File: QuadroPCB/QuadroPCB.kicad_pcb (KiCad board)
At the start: 2 copper layers, 80 x 119.4 mm, 23 parts, among them IC1 AT24CS02-SSHM, P1 MPU9150, P10 AKKU, P2 stm32discovery_left, P3 stm32discovery_right, P4 rc_signal, P5 Motor3, P6 Motor4, P7 BMP180, P8 Motor1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

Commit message: dei mudder commitet
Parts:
- P10: footprint Wire_Connections_Bridges:WireConnection_1-2mmDrill -> Connect:PINHEAD1-2
- moved R4 15.9 mm to (108.0, 107.3), turned to 90 degrees
- moved Q1 14.8 mm to (108.0, 98.4), turned to 270 degrees
- moved P1 12.0 mm to (72.4, 146.1)
- moved IC1 11.4 mm to (94.0, 142.2), turned to 90 degrees
- moved P7 10.2 mm to (86.4, 166.4)
- moved SP1 6.35 mm to (100.3, 76.2)
- moved R5 4.62 mm to (98.4, 168.9)
- moved R3 2.29 mm to (101.0, 168.9)
- moved P10 1.27 mm to (58.4, 74.9)
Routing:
- net GND: track 38.6 -> 445.8 mm
- net +3V3: track 0.00 -> 174.3 mm
- net +5V: track 30.8 -> 83.3 mm
- net +BATT: track 28.6 -> 73.1 mm
- net I2C1_SDA: track 0.00 -> 38.7 mm
- net I2C1_SCL: track 0.00 -> 36.7 mm
- net PE4: track 0.00 -> 33.0 mm
- net I2C2_SCL: track 0.00 -> 24.1 mm
- net Net-(Q1-Pad3): track 0.00 -> 23.2 mm
- net MOTOR2: track 0.00 -> 22.4 mm
- net I2C2_SDA: track 0.00 -> 22.2 mm
- net PC9: track 0.00 -> 15.9 mm
- net MOTOR3: track 0.00 -> 14.7 mm
- net MOTOR1: track 0.00 -> 13.8 mm
- net RC_Signal: track 0.00 -> 13.8 mm
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- added copper zone on B.Cu, net GND
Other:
- net class Default: clearance 0.254 -> 0.25
- net class bla: clearance 0.254 -> 0.25
- rule trace_clearance: 0.254 -> 0.25

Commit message: neuer step down
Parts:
- added C3: 10nF, Capacitors_SMD:C_0805_HandSoldering, B.Cu at (81.9, 97.2)
- C1: value 100µ 25V -> 220µF 25V; footprint Capacitors_SMD:c_elec_6.3x7.7 -> Capacitors_SMD:c_elec_8x10.5
- C2: value 680µF 10V -> 100µF 10V; footprint Capacitors_SMD:c_elec_8x10 -> Capacitors_SMD:c_elec_8x6.7
- D1: value MBR360 -> MBRS340; footprint Diodes_SMD:Diode-DO-214BA -> Diodes_SMD:Diode-DO-214AB_Handsoldering
- L1: value 220µH -> 33µH 1,4 A; footprint Choke_SMD:Choke_SMD_PISR_Handsoldering_FASTRON -> Choke_SMD:Choke_SMD_PISN_Handsoldering_FASTRON
- U1: value LM2576S-5 -> LM2675M-5; footprint SMD_Packages:TO-263-5_HandSoldering -> SMD_Packages:SOIC-8-N
- moved U1 16.2 mm to (81.9, 102.2)
- moved C2 16.2 mm to (88.3, 111.1), turned to 0 degrees
- moved C1 8.28 mm to (65.4, 88.3), turned to 0 degrees
- moved D1 7.85 mm to (71.8, 101.6)
- moved R1 7.73 mm to (50.8, 118.1), turned to 270 degrees
- moved L1 6.54 mm to (81.9, 88.3)
- moved P10 4.49 mm to (62.9, 75.6), turned to 0 degrees
- moved R2 2.29 mm to (49.5, 122.6), turned to 180 degrees
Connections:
- net I2C2_SDA renamed PA10
- net MOTOR2 renamed PC7
- net MOTOR3 renamed PC8
- net PE4 renamed MPU9150_INT
- D1 pad 1: /pwr -> Net-(C3-Pad1)
- L1 pad 1: /pwr -> Net-(C3-Pad1)
- U1 pad 1: +BATT -> Net-(C3-Pad2)
- U1 pad 2: /pwr -> (no net)
- U1 pad 3: GND -> (no net)
- U1 pad 5: GND -> Net-(U1-Pad5)
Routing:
- net GND: track 445.8 -> 365.2 mm
- net +5V: track 83.3 -> 50.4 mm
- net Net-(C3-Pad1): track 0.00 -> 27.2 mm
- net /pwr: track 18.0 -> 0.00 mm
- net Net-(C3-Pad2): track 0.00 -> 3.97 mm
- net +3V3: track 174.3 -> 172.1 mm
- net +BATT: track 73.1 -> 73.9 mm, vias 0 -> 2
- net ADC_Akkumonitor: track 7.49 -> 8.17 mm
- added copper zone on B.Cu, net +5V
- added copper zone on B.Cu, net Net-(C3-Pad1)

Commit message: blubb
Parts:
- added P11: MeisterFluglicht, Pin_Headers:Pin_Header_Straight_1x05, F.Cu at (72.4, 153.7)
- added Q2: Q_NMOS_GSD, Housings_SOT-23_SOT-143_TSOT-6:SOT-23_Handsoldering, B.Cu at (110.5, 106.7)
- added R6: 1k, Resistors_SMD:R_0805_HandSoldering, B.Cu at (111.8, 113.0)
- added SP2: SPEAKER, Buzzers_Beepers:Buzzer_12x9.5RM7.6, B.Cu at (100.3, 104.1)
- SP1: moved to B.Cu
- moved SP1 12.7 mm to (100.3, 88.9), turned to 270 degrees
- moved R4 11.9 mm to (113.0, 118.1), turned to 0 degrees
- moved C3 5.08 mm to (76.8, 97.2)
- moved L1 5.08 mm to (76.8, 88.3)
- moved U1 5.08 mm to (76.8, 102.2)
- moved P10 5.08 mm to (57.8, 75.6)
- moved C1 5.08 mm to (60.3, 88.3)
- moved C2 5.08 mm to (83.2, 111.1)
- moved D1 5.08 mm to (66.7, 101.6)
- moved Q1 3.17 mm to (108.0, 95.2), turned to 180 degrees
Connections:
- net I2C1_SCL renamed PB6
- net MOTOR1 renamed PC6
- net MPU9150_INT renamed PE4
- net PA10 renamed I2C2_SDA
- net PC8 renamed MOTOR3
- P2 pad 35: Net-(P2-Pad35) -> PB13
- P2 pad 36: Net-(P2-Pad36) -> PB12
- P2 pad 37: Net-(P2-Pad37) -> LEDS_SPI_MOSI
- P2 pad 38: Net-(P2-Pad38) -> LEDS_SPI_MISO
- P3 pad 3: Net-(P3-Pad3) -> Beeper1_PIN
- P3 pad 4: Net-(P3-Pad4) -> Beeper2_PIN
- R4 pad 1: Beeper_PIN -> Beeper2_PIN
- SP1 pad 1: Net-(Q1-Pad3) -> +5V
- SP1 pad 2: +5V -> Net-(Q1-Pad3)
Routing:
- net GND: track 365.2 -> 525.6 mm
- net +5V: track 50.4 -> 89.0 mm
- net PB13: track 0.00 -> 19.9 mm
- net LEDS_SPI_MOSI: track 0.00 -> 18.8 mm
- net PB12: track 0.00 -> 16.3 mm
- net LEDS_SPI_MISO: track 0.00 -> 15.2 mm
- net Net-(Q1-Pad3): track 23.2 -> 8.05 mm
- net Net-(Q1-Pad1): track 9.81 -> 23.6 mm
- net Net-(Q2-Pad3): track 0.00 -> 11.3 mm
- net Beeper1_PIN: track 0.00 -> 7.90 mm
- net +BATT: track 73.9 -> 69.1 mm
- net Beeper2_PIN: track 0.00 -> 3.73 mm
- net Net-(Q2-Pad1): track 0.00 -> 3.63 mm

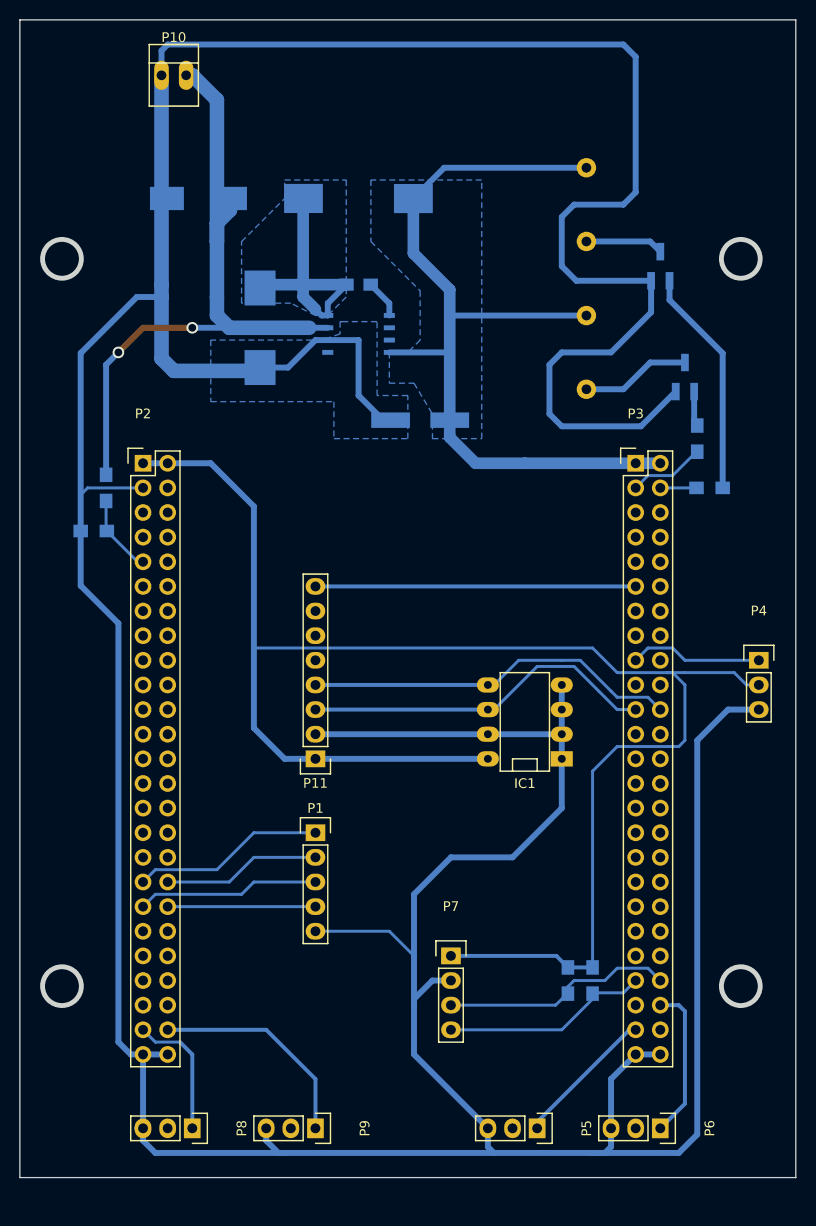
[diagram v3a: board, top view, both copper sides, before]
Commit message: step down extern fluglicht auf die platine gepackt
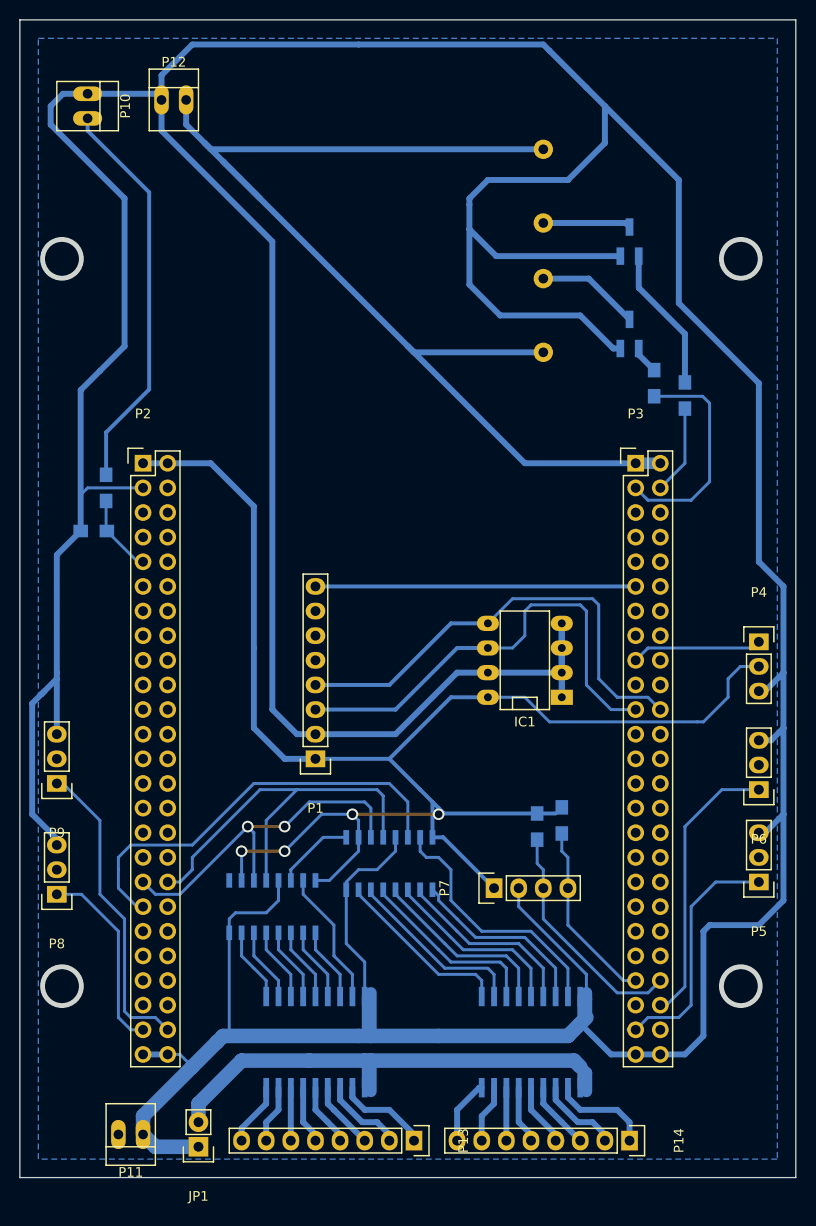
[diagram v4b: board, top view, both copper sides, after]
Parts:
- removed C1: 220µF 25V, Capacitors_SMD:c_elec_8x10.5
- removed C2: 100µF 10V, Capacitors_SMD:c_elec_8x6.7
- removed C3: 10nF, Capacitors_SMD:C_0805_HandSoldering
- removed D1: MBRS340, Diodes_SMD:Diode-DO-214AB_Handsoldering
- removed L1: 33µH 1,4 A, Choke_SMD:Choke_SMD_PISN_Handsoldering_FASTRON
- added JP1: led_test, Pin_Headers:Pin_Header_Straight_1x02, F.Cu at (60.3, 186.1)
- added P12: step_down, Connect:PINHEAD1-2, F.Cu at (57.8, 78.1)
- added P13: leds1, Pin_Headers:Pin_Header_Straight_1x08, F.Cu at (82.5, 185.4)
- added P14: leds2, Pin_Headers:Pin_Header_Straight_1x08, F.Cu at (104.8, 185.4)
- added U2: 74HC595, Housings_SOIC:SOIC-16_3.9x9.9mm_Pitch1.27mm, B.Cu at (80.0, 156.8)
- added U3: uln2803, Housings_SOIC:SOIC-18_7.5x11.6mm_Pitch1.27mm, B.Cu at (72.4, 175.3)
- added U4: uln2803, Housings_SOIC:SOIC-18_7.5x11.6mm_Pitch1.27mm, B.Cu at (94.6, 175.3)
- P11: value MeisterFluglicht -> led_power; footprint Pin_Headers:Pin_Header_Straight_1x05 -> Connect:PINHEAD1-2
- U1: value LM2675M-5 -> 74HC595; footprint SMD_Packages:SOIC-8-N -> Housings_SOIC:SOIC-16_3.9x9.9mm_Pitch1.27mm
- moved U1 59.7 mm to (67.9, 161.3), turned to 90 degrees
- moved P9 44.5 mm to (45.7, 148.6), turned to 180 degrees
- moved P11 36.5 mm to (53.3, 184.8), turned to 180 degrees
- moved P6 36.4 mm to (118.1, 149.2), turned to 180 degrees
- moved P5 34.2 mm to (118.1, 158.8), turned to 180 degrees
- moved P8 27.9 mm to (45.7, 160.0), turned to 180 degrees
- moved R3 16.8 mm to (97.8, 152.4)
- moved R5 16.2 mm to (95.2, 153.0)
- moved R4 9.86 mm to (110.5, 108.6), turned to 90 degrees
- moved P10 9.44 mm to (48.9, 78.7), turned to 270 degrees
- moved P7 8.28 mm to (90.8, 159.4), turned to 90 degrees
- moved R6 7.24 mm to (107.3, 107.3)
- moved Q2 7.24 mm to (104.8, 102.2)
- moved IC1 6.35 mm to (94.0, 135.9)
- moved SP2 5.85 mm to (95.9, 100.3), turned to 90 degrees
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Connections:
- net Beeper2_PIN renamed PF10
- net I2C2_SCL renamed PA9
- net PB6 renamed I2C1_SCL
- net PC6 renamed MOTOR1
- net PC7 renamed MOTOR2
- net PE4 renamed MPU9150_INT
- P11 pad 1: PB13 -> GND
- P11 pad 2: PB12 -> Net-(P11-Pad2)
- P2 pad 35: PB13 -> LEDS_SPI_SCK
- P2 pad 36: PB12 -> LEDS_RCK
- P2 pad 38: LEDS_SPI_MISO -> PB14
- U1 pad 2: (no net) -> Net-(U1-Pad2)
- U1 pad 3: (no net) -> Net-(U1-Pad3)
- U1 pad 4: +5V -> Net-(U1-Pad4)
- U1 pad 6: GND -> Net-(U1-Pad6)
- U1 pad 7: +BATT -> Net-(U1-Pad7)
- U1 pad 8: Net-(C3-Pad1) -> GND
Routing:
- net GND: track 525.6 -> 623.0 mm
- net Net-(JP1-Pad2): track 0.00 -> 55.6 mm
- net LEDS_RCK: track 0.00 -> 42.1 mm
- net LEDS_SPI_SCK: track 0.00 -> 37.1 mm, vias 0 -> 2
- net +5V: track 89.0 -> 120.7 mm
- net +BATT: track 69.1 -> 41.9 mm, vias 2 -> 0
- net Net-(C3-Pad1): track 27.2 -> 0.00 mm
- net Net-(U2-Pad15): track 0.00 -> 26.4 mm
- net LEDS_SPI_MOSI: track 18.8 -> 43.9 mm
- net PB13: track 19.9 -> 0.00 mm
- net Net-(U2-Pad5): track 0.00 -> 19.3 mm
- net Net-(U2-Pad4): track 0.00 -> 19.3 mm
- net Net-(U2-Pad2): track 0.00 -> 19.3 mm
- net Net-(U2-Pad3): track 0.00 -> 19.3 mm
- net Net-(U2-Pad1): track 0.00 -> 19.3 mm
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- removed copper zone on B.Cu, net +5V
- removed copper zone on B.Cu, net Net-(C3-Pad1)

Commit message: version 1
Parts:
- IC1: value AT24CS02-SSHM -> EEPROM
- P11: value led_power -> LED Power
- P12: value step_down -> +5V
- P13: value leds1 -> (none); footprint Pin_Headers:Pin_Header_Straight_1x08 -> Pin_Headers:Pin_Header_Straight_2x08
- P14: value leds2 -> (none); footprint Pin_Headers:Pin_Header_Straight_1x08 -> Pin_Headers:Pin_Header_Straight_2x08
- P4: value rc_signal -> RC Signal
- moved JP1 1.27 mm to (60.3, 184.8)
- moved R1 0.63 mm to (50.2, 118.1)
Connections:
- net I2C2_SDA renamed PA10
- net MOTOR2 renamed PC7
- net MPU9150_INT renamed PE4
- net PC9 renamed MOTOR4
- net RC_Signal renamed PB8
- P13 pad 2: Net-(P13-Pad2) -> Net-(P11-Pad2)
- P13 pad 4: Net-(P13-Pad4) -> Net-(P11-Pad2)
- P13 pad 6: Net-(P13-Pad6) -> Net-(P11-Pad2)
- P13 pad 8: Net-(P13-Pad8) -> Net-(P11-Pad2)
- P14 pad 2: Net-(P14-Pad2) -> Net-(P11-Pad2)
- P14 pad 4: Net-(P14-Pad4) -> Net-(P11-Pad2)
- P14 pad 6: Net-(P14-Pad6) -> Net-(P11-Pad2)
- P14 pad 8: Net-(P14-Pad8) -> Net-(P11-Pad2)
- U3 pad 12: Net-(P13-Pad2) -> Net-(P13-Pad3)
- U3 pad 13: Net-(P13-Pad3) -> Net-(P13-Pad5)
- U3 pad 14: Net-(P13-Pad4) -> Net-(P13-Pad7)
- U3 pad 15: Net-(P13-Pad5) -> Net-(P13-Pad9)
- U3 pad 16: Net-(P13-Pad6) -> Net-(P13-Pad11)
- U3 pad 17: Net-(P13-Pad7) -> Net-(P13-Pad13)
- U3 pad 18: Net-(P13-Pad8) -> Net-(P13-Pad15)
- U4 pad 12: Net-(P14-Pad2) -> Net-(P14-Pad3)
- U4 pad 13: Net-(P14-Pad3) -> Net-(P14-Pad5)
- U4 pad 14: Net-(P14-Pad4) -> Net-(P14-Pad7)
- U4 pad 15: Net-(P14-Pad5) -> Net-(P14-Pad9)
- U4 pad 16: Net-(P14-Pad6) -> Net-(P14-Pad11)
- U4 pad 17: Net-(P14-Pad7) -> Net-(P14-Pad13)
- U4 pad 18: Net-(P14-Pad8) -> Net-(P14-Pad15)
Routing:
- net Net-(P11-Pad2): track 0.00 -> 55.7 mm
- net GND: track 623.0 -> 640.0 mm
- net Net-(P14-Pad2): track 8.46 -> 0.00 mm
- net Net-(P13-Pad2): track 8.46 -> 0.00 mm
- net Net-(P14-Pad4): track 6.78 -> 0.00 mm
- net Net-(P14-Pad8): track 6.66 -> 0.00 mm
- net Net-(P14-Pad15): track 0.00 -> 6.66 mm
- net Net-(P13-Pad8): track 6.51 -> 0.00 mm
- net Net-(P13-Pad4): track 6.51 -> 0.00 mm
- net Net-(P13-Pad15): track 0.00 -> 6.51 mm
- net Net-(P14-Pad13): track 0.00 -> 5.99 mm
- net Net-(P13-Pad13): track 0.00 -> 5.99 mm
- net Net-(P14-Pad9): track 0.00 -> 5.99 mm
- net Net-(P13-Pad9): track 0.00 -> 5.99 mm
- net Net-(P14-Pad6): track 5.46 -> 0.00 mm
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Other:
- board size 80 x 119.4 mm -> 80 x 121.9 mm
- board text added: "+"
- board text added: "1 2 3 4 5 6 7 8"
- board text added: "9 10 11 12 13 14 15 16"
- board text added: "LEDs"
- board text added: "Vcc"
- board text added: "gnd"
